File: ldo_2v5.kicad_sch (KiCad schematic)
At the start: 6 parts, among them U4 TPS7A20

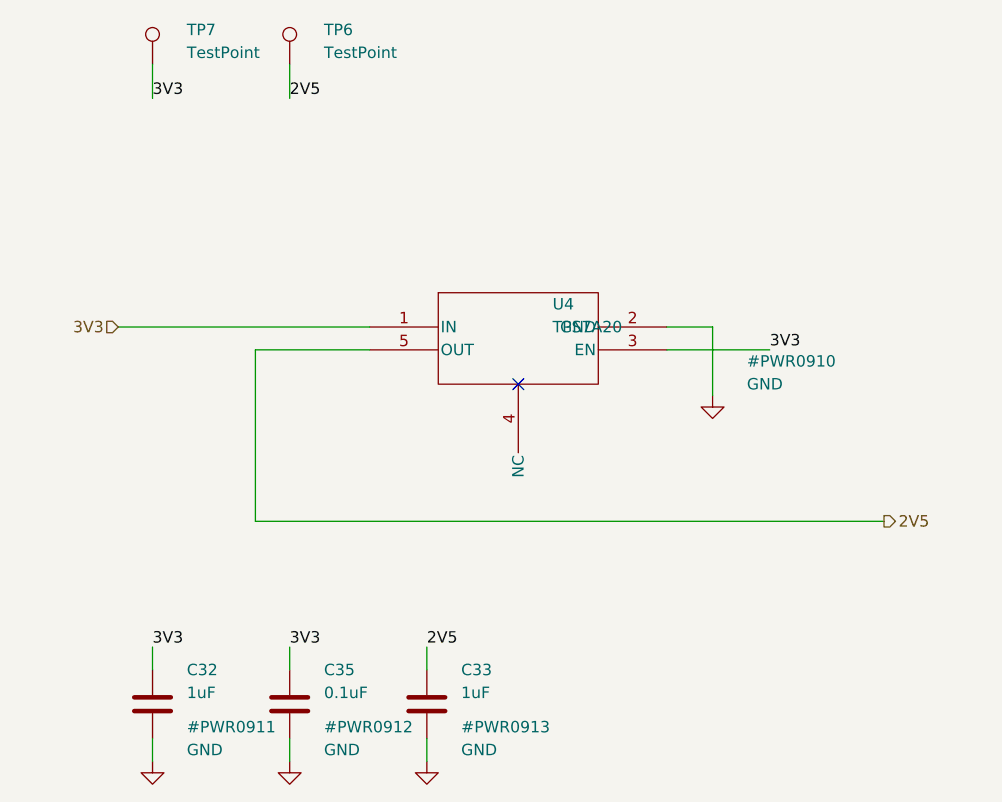
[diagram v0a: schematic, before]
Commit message: Migrate LDO sheets to KL library symbols
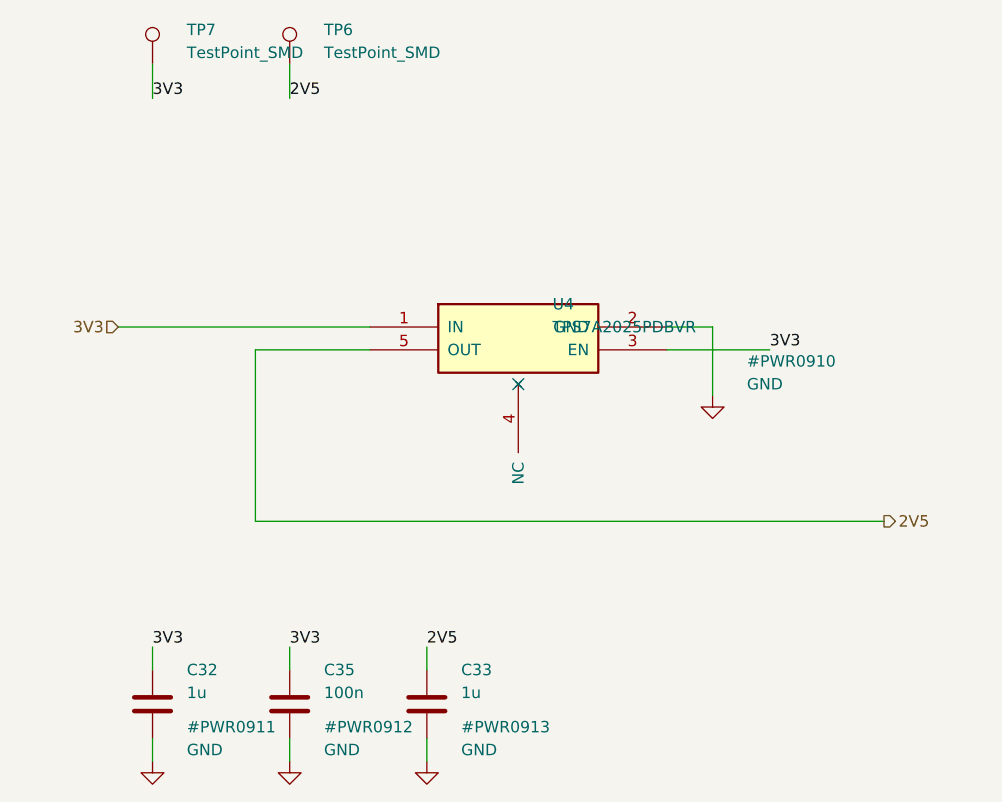
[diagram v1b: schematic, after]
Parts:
- C32, C33: value 1uF -> 1u; footprint Capacitor_SMD:C_0402_1005Metric_Pad0.74x0.62mm_HandSolder -> KL_Footprints:C_0402; symbol Device:C -> KL_C:C_1u_16V_10pct_X5R_0402; Dielectric (none) -> X5R; Digikey (none) -> TBD; LCSC (none) -> TBD; MPN (none) -> GRM155R61C105KA12D; Mouser (none) -> 81-GRM155R61C105KA12D; Package_in_inch (none) -> 0402; Tolerance_in_pct (none) -> 10; Voltage_in_V (none) -> 16
- C35: value 0.1uF -> 100n; footprint Capacitor_SMD:C_0402_1005Metric_Pad0.74x0.62mm_HandSolder -> KL_Footprints:C_0402; symbol Device:C -> KL_C:C_100n_35V_10pct_X7R_0402; Dielectric (none) -> X7R; Digikey (none) -> 445-6901-1-ND; LCSC (none) -> C2181802; MPN (none) -> CGA2B3X7R1V104K050BB; Mouser (none) -> 810-CGA2B3X7R1V104K; Package_in_inch (none) -> 0402; Tolerance_in_pct (none) -> 10; Voltage_in_V (none) -> 35
- TP6, TP7: value TestPoint -> TestPoint_SMD; footprint TestPoint:TestPoint_Pad_1.0x1.0mm -> KL_Footprints:TestPoint_SMD_1.0x1.0mm; symbol Connector:TestPoint -> KL_TestPoint:TestPoint_SMD
- U4: value TPS7A20 -> TPS7A2025PDBVR; footprint Package_TO_SOT_SMD:SOT-23-5 -> KL_Footprints:SOT-23-5; symbol TPS7A20C:TPS7A20C285PYCKR -> KL_Voltage_Regulators:TPS7A2025PDBVR; Digikey (none) -> TBD; I_OUT_A (none) -> 0.3; I_VIN_A (none) -> TBD; LCSC (none) -> TBD; MPN (none) -> TPS7A2025PDBVR; Mouser (none) -> 595-TPS7A2025PDBVR; VIN_MAX_V (none) -> 6.5; VIN_MIN_V (none) -> 1.6; V_OUT_V (none) -> 2.5

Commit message: Apply signal naming convention to all nets
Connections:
- net 2V5 renamed VDD_2V5
- net 3V3 renamed VDD_3V3
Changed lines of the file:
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@@
 		)
 	)
-	(hierarchical_label "3V3"
+	(hierarchical_label "VDD_3V3"
 		(shape input)
 		(at 96.52 88.9 180)
@@
 		)
 	)
-	(hierarchical_label "2V5"
+	(hierarchical_label "VDD_2V5"
 		(shape output)
 		(at 181.61 110.49 0)
@@
 		)
 	)
-	(label "3V3"
+	(label "VDD_3V3"
 		(at 168.91 91.44 0)
 		(effects
@@
 		)
 	)
-	(label "3V3"
+	(label "VDD_3V3"
 		(at 100.33 124.46 0)
 		(effects
@@
 		)
 	)
-	(label "3V3"
+	(label "VDD_3V3"
 		(at 115.57 124.46 0)
 		(effects
@@
 		)
 	)
-	(label "2V5"
+	(label "VDD_2V5"
 		(at 130.81 124.46 0)
 		(effects
@@
 		)
 	)
-	(label "3V3"
+	(label "VDD_3V3"
 		(at 100.33 63.5 0)
 		(effects
@@
 		)
 	)
-	(label "2V5"
+	(label "VDD_2V5"
 		(at 115.57 63.5 0)
 		(effects

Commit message: Improve schematic readability across all sheets
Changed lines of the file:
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@@
 		(dnp no)
 		(property "Reference" "U4"
-			(at 144.78 86.36 0)
-			(effects
-				(font
-					(size 1.27 1.27)
-				)
-				(justify left)
+			(at 140.97 81.28 0)
+			(effects
+				(font
+					(size 1.27 1.27)
+				)
 			)
 		)
 		(property "Value" "TPS7A2025PDBVR"
-			(at 144.78 88.9 0)
-			(effects
-				(font
-					(size 1.27 1.27)
-				)
-				(justify left)
+			(at 140.97 83.82 0)
+			(effects
+				(font
+					(size 1.27 1.27)
+				)
 			)
 		)
@@
 		(property "Reference" "#PWR0910"
 			(at 166.37 92.71 0)
+			(hide yes)
 			(effects
 				(font
@@
 		(property "Reference" "#PWR0911"
 			(at 104.14 133.35 0)
+			(hide yes)
 			(effects
 				(font
@@
 		(property "Reference" "#PWR0912"
 			(at 119.38 133.35 0)
+			(hide yes)
 			(effects
 				(font
@@
 		(property "Reference" "#PWR0913"
 			(at 134.62 133.35 0)
+			(hide yes)
 			(effects
 				(font
@@
 		(property "Value" "TestPoint_SMD"
 			(at 104.14 58.419999999999995 0)
+			(hide yes)
 			(effects
 				(font
@@
 		(property "Value" "TestPoint_SMD"
 			(at 119.38 58.419999999999995 0)
-			(effects
-				(font
+			(hide yes)
+			(effects
+				(font

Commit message: Move 2V5 LDO ground symbol; KiCad 10 format
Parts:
- C32, C33: Digikey TBD -> 490-10694-1-ND; LCSC TBD -> C77006
- U4: Digikey TBD -> 296-TPS7A2025PDBVRCT-ND; LCSC TBD -> C2869949
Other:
- company: (none) -> Kebag Logic: kebag-logic.com
- title: (none) -> LDO 2V5

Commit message: Switch BOM to in-stock LCSC parts, U3 to TLV73311
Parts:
- C35: Digikey 445-6901-1-ND -> (none); LCSC C2181802 -> C307331; MPN CGA2B3X7R1V104K050BB -> CL05B104KB54PNC; Mouser 810-CGA2B3X7R1V104K -> (none); Voltage_in_V 35 -> 50
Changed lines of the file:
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@@
 			)
 		)
-		(property "Datasheet" "https://product.tdk.com/system/files/dam/doc/product/capacitor/ceramic/mlcc/catalog/mlcc_automotive_general_en.pdf"
+		(property "Datasheet" "https://www.lcsc.com/datasheet/lcsc_datasheet_2304140030_Samsung-Electro-Mechanics-CL05B104KB54PNC_C307331.pdf"
 			(at 119.38 134.62 0)
 			(hide yes)
@@
 			)
 		)
-		(property "Voltage_in_V" "35"
+		(property "Voltage_in_V" "50"
 			(at 0 0 0)
 			(hide yes)
@@
 			)
 		)
-		(property "MPN" "CGA2B3X7R1V104K050BB"
+		(property "MPN" "CL05B104KB54PNC"
 			(at 0 0 0)
 			(hide yes)
@@
 			)
 		)
-		(property "Mouser" "810-CGA2B3X7R1V104K"
+		(property "Mouser" ""
 			(at 0 0 0)
 			(hide yes)
@@
 			)
 		)
-		(property "Digikey" "445-6901-1-ND"
+		(property "Digikey" ""
 			(at 0 0 0)
 			(hide yes)
@@
 			)
 		)
-		(property "LCSC" "C2181802"
+		(property "LCSC" "C307331"
 			(at 0 0 0)
 			(hide yes)
